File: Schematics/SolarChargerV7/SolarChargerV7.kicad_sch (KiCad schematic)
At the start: 24 parts, among them J1 USB_A, Q1 CSD16410Q5A, U1 LM3478MA_NOPB

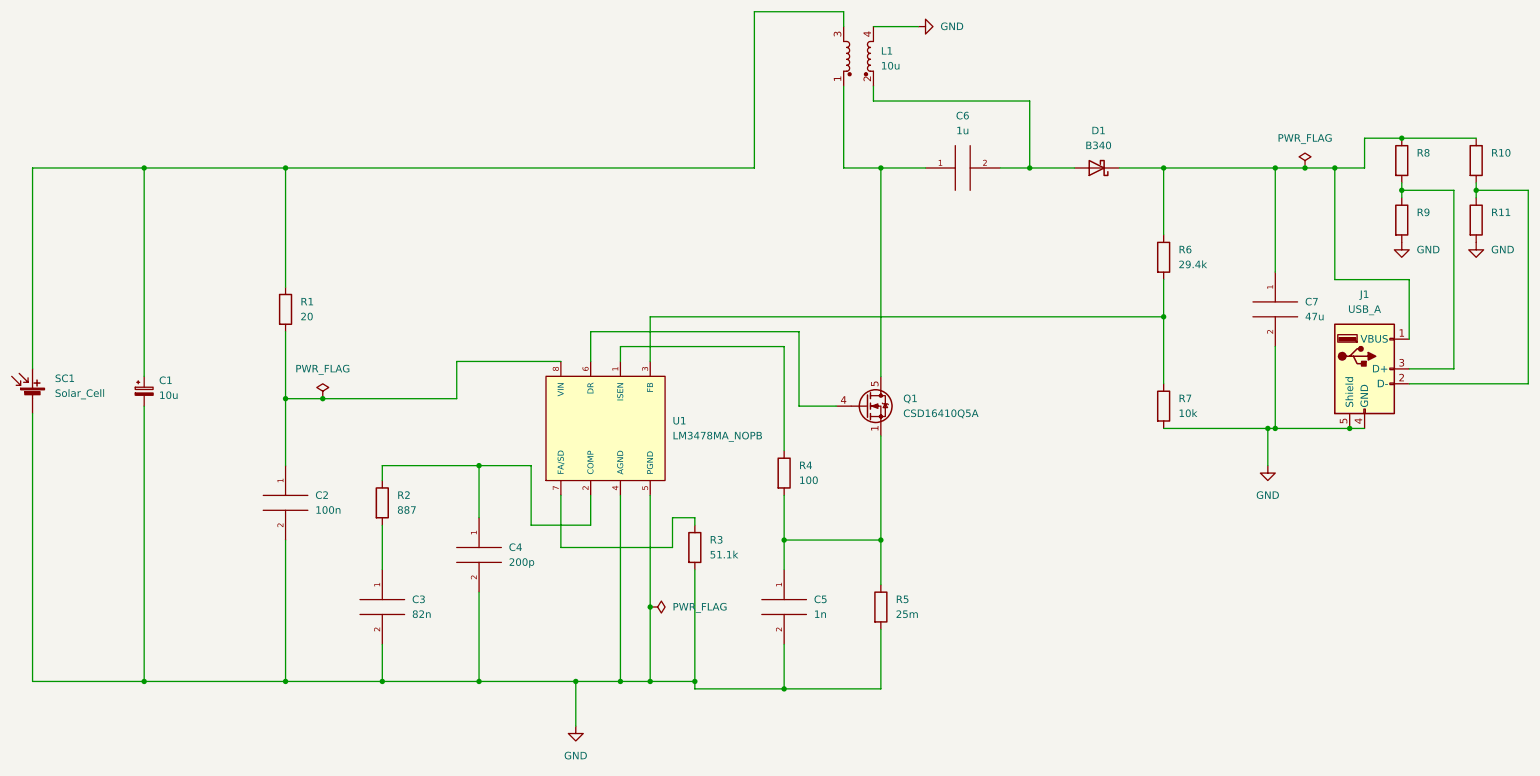
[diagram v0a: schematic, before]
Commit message: quick fix of resistor values for voltage divider
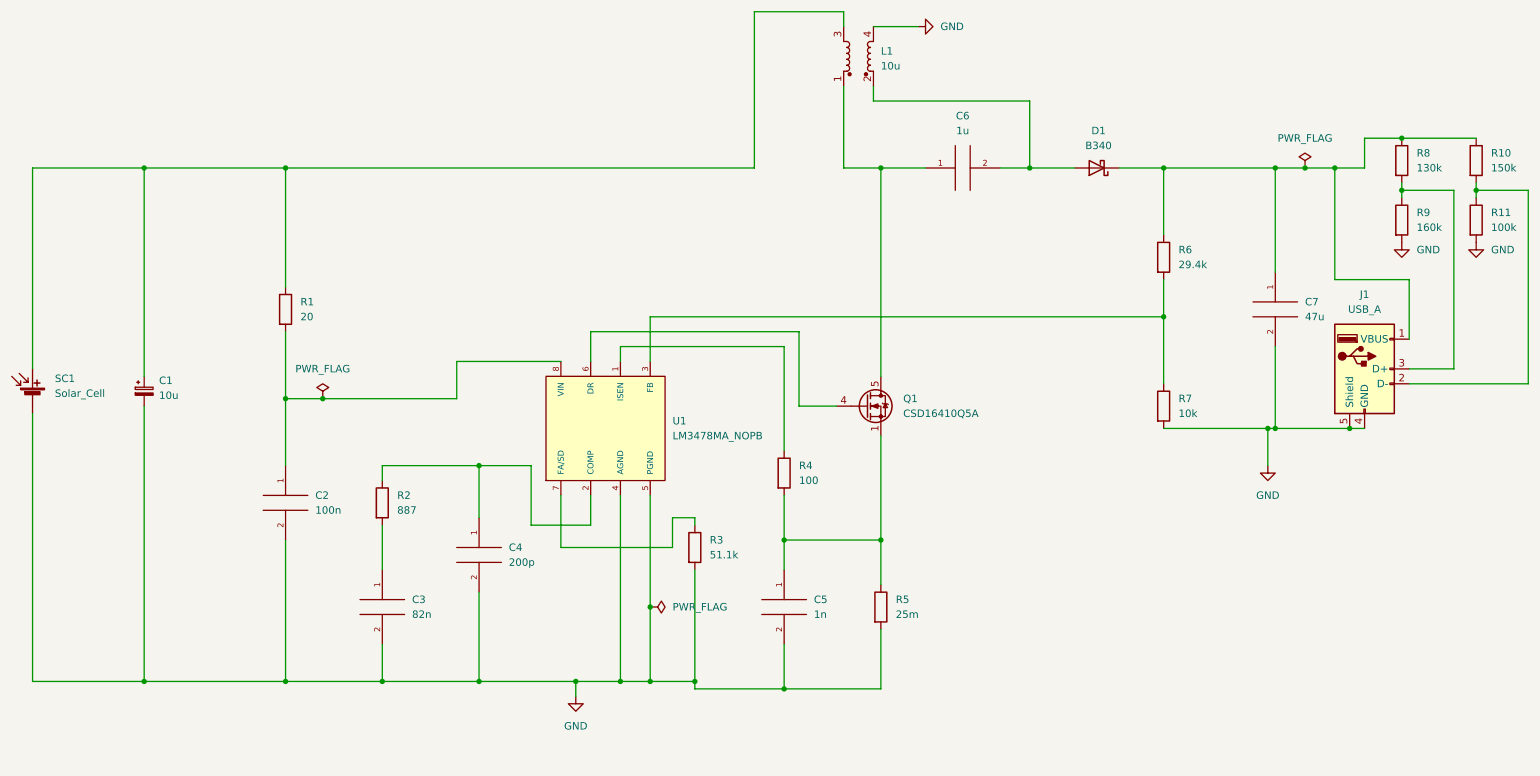
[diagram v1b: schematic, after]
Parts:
- R10: value (none) -> 150k; footprint (none) -> Resistor_SMD:R_0805_2012Metric
- R11: value (none) -> 100k; footprint (none) -> Resistor_SMD:R_0805_2012Metric
- R8: value (none) -> 130k; footprint (none) -> Resistor_SMD:R_0805_2012Metric
- R9: value (none) -> 160k; footprint (none) -> Resistor_SMD:R_0805_2012Metric
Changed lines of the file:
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@@
     (stroke (width 0) (type default) (color 0 0 0 0))
   )
-  (wire (pts (xy 115.57 154.94) (xy 115.57 162.56))
+  (wire (pts (xy 115.57 154.94) (xy 115.57 157.48))
     (stroke (width 0) (type default) (color 0 0 0 0))
   )
@@
       (effects (font (size 1.27 1.27)) (justify left))
     )
-    (property "Value" "" (id 1) (at 259.08 77.4699 0)
-      (effects (font (size 1.27 1.27)) (justify left))
-    )
-    (property "Footprint" "" (id 2) (at 254.762 76.2 90)
+    (property "Value" "160k" (id 1) (at 259.08 77.4699 0)
+      (effects (font (size 1.27 1.27)) (justify left))
+    )
+    (property "Footprint" "Resistor_SMD:R_0805_2012Metric" (id 2) (at 254.762 76.2 90)
       (effects (font (size 1.27 1.27)) hide)
     )
@@
       (effects (font (size 1.27 1.27)) (justify left))
     )
-    (property "Value" "" (id 1) (at 271.78 67.3099 0)
-      (effects (font (size 1.27 1.27)) (justify left))
-    )
-    (property "Footprint" "" (id 2) (at 267.462 66.04 90)
+    (property "Value" "150k" (id 1) (at 271.78 67.3099 0)
+      (effects (font (size 1.27 1.27)) (justify left))
+    )
+    (property "Footprint" "Resistor_SMD:R_0805_2012Metric" (id 2) (at 267.462 66.04 90)
       (effects (font (size 1.27 1.27)) hide)
     )
@@
       (effects (font (size 1.27 1.27)) (justify left))
     )
-    (property "Value" "" (id 1) (at 271.78 77.4699 0)
-      (effects (font (size 1.27 1.27)) (justify left))
-    )
-    (property "Footprint" "" (id 2) (at 267.462 76.2 90)
+    (property "Value" "100k" (id 1) (at 271.78 77.4699 0)
+      (effects (font (size 1.27 1.27)) (justify left))
+    )
+    (property "Footprint" "Resistor_SMD:R_0805_2012Metric" (id 2) (at 267.462 76.2 90)
       (effects (font (size 1.27 1.27)) hide)
     )
@@
     (pin "1")
   )
-  (symbol (lib_id "power:GND") (at 115.57 162.56 0) (unit 1)
-    (in_bom yes) (on_board yes) (fields_autoplaced)
-    (property "Reference" "#PWR0102" (id 0) (at 115.57 168.91 0)
-      (effects (font (size 1.27 1.27)) hide)
-    )
-    (property "Value" "GND" (id 1) (at 115.57 167.64 0))
-    (property "Footprint" "" (id 2) (at 115.57 162.56 0)
-      (effects (font (size 1.27 1.27)) hide)
-    )
-    (property "Datasheet" "" (id 3) (at 115.57 162.56 0)
+  (symbol (lib_id "power:GND") (at 115.57 157.48 0) (unit 1)
+    (in_bom yes) (on_board yes) (fields_autoplaced)
+    (property "Reference" "#PWR0102" (id 0) (at 115.57 163.83 0)
+      (effects (font (size 1.27 1.27)) hide)
+    )
+    (property "Value" "GND" (id 1) (at 115.57 162.56 0))
+    (property "Footprint" "" (id 2) (at 115.57 157.48 0)
+      (effects (font (size 1.27 1.27)) hide)
+    )
+    (property "Datasheet" "" (id 3) (at 115.57 157.48 0)
       (effects (font (size 1.27 1.27)) hide)
     )
@@
       (effects (font (size 1.27 1.27)) (justify left))
     )
-    (property "Value" "" (id 1) (at 259.08 67.3099 0)
-      (effects (font (size 1.27 1.27)) (justify left))
-    )
-    (property "Footprint" "" (id 2) (at 254.762 66.04 90)
+    (property "Value" "130k" (id 1) (at 259.08 67.3099 0)
+      (effects (font (size 1.27 1.27)) (justify left))
+    )
+    (property "Footprint" "Resistor_SMD:R_0805_2012Metric" (id 2) (at 254.762 66.04 90)
       (effects (font (size 1.27 1.27)) hide)
     )
@@
     )
     (path "/b9873c4a-4015-496c-92a0-d27424f65a77"
-      (reference "R8") (unit 1) (value "150k") (footprint "Resistor_SMD:R_0805_2012Metric")
+      (reference "R8") (unit 1) (value "130k") (footprint "Resistor_SMD:R_0805_2012Metric")
     )
     (path "/385c99ae-608b-485d-8179-68db64be0870"
-      (reference "R9") (unit 1) (value "100k") (footprint "Resistor_SMD:R_0805_2012Metric")
+      (reference "R9") (unit 1) (value "160k") (footprint "Resistor_SMD:R_0805_2012Metric")
     )
     (path "/8c04a86f-bffd-4d18-a144-5a58d5edcc4e"
-      (reference "R10") (unit 1) (value "130k") (footprint "Resistor_SMD:R_0805_2012Metric")
+      (reference "R10") (unit 1) (value "150k") (footprint "Resistor_SMD:R_0805_2012Metric")
     )
     (path "/914764c3-8c4f-44e2-801b-746a70e36ff9"
-      (reference "R11") (unit 1) (value "160k") (footprint "Resistor_SMD:R_0805_2012Metric")
+      (reference "R11") (unit 1) (value "100k") (footprint "Resistor_SMD:R_0805_2012Metric")
     )
     (path "/fd955970-c990-4603-96b5-f465442bdb88"
